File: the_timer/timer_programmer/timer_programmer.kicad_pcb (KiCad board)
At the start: 2 copper layers, 18 x 23.5 mm, 6 parts, among them J1 AVR-ISP-6, J3 R41-B583A, U1 MCP2210x-SS

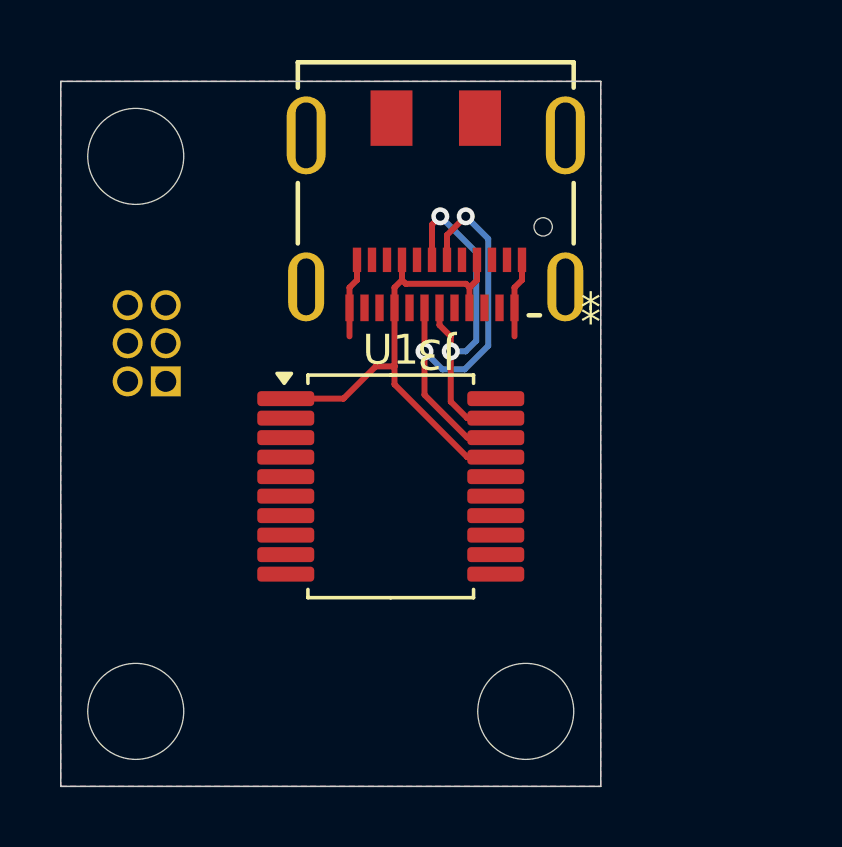
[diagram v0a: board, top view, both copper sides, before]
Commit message: Finished routing Timer Programmer
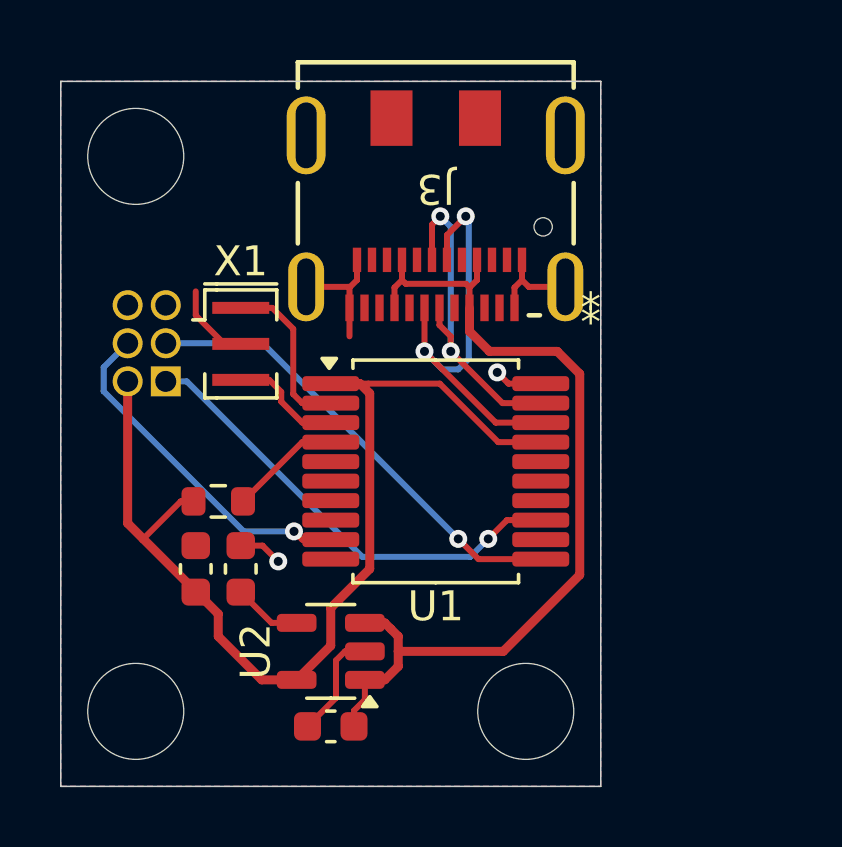
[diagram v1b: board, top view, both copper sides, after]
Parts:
- added C2: 1u, Capacitor_SMD:C_0603_1608Metric, F.Cu at (209.0, 98.0)
- added C3: 0.01u, Capacitor_SMD:C_0603_1608Metric, F.Cu at (206.0, 92.8)
- added C4: 1u, Capacitor_SMD:C_0603_1608Metric, F.Cu at (204.5, 92.8)
- added R1: 10k, Resistor_SMD:R_0603_1608Metric, F.Cu at (205.2, 90.5)
- added U2: TC2185-3.3VxCTTR, Package_TO_SOT_SMD:SOT-23-5, F.Cu at (209.0, 95.5)
- added X1: CSTNE12M0GH5L000R0, Crystal:Resonator_SMD_Murata_CSTxExxV-3Pin_3.0x1.1mm, F.Cu at (206.0, 85.2)
- moved U1 1.58 mm to (212.5, 89.5)
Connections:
- J3 pad A4: VCC -> VBUS
- J3 pad A9: VCC -> VBUS
- J3 pad B4: VCC -> VBUS
- J3 pad B9: VCC -> VBUS
- U1 pad 2: unconnected-(U1-OSC1-Pad2) -> Net-(U1-OSC1)
- U1 pad 3: unconnected-(U1-OSC2-Pad3) -> Net-(U1-OSC2)
- U1 pad 4: ~{RESET} -> Net-(U1-~{RST})
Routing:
- net VBUS: track 0.00 -> 29.9 mm
- net VCC: track 16.8 -> 35.0 mm
- net MISO: track 0.00 -> 16.4 mm, vias 0 -> 1
- net SCLK: track 0.00 -> 15.5 mm, vias 0 -> 1
- net MOSI: track 0.00 -> 12.1 mm, vias 0 -> 1
- net GND: track 5.30 -> 16.8 mm, vias 0 -> 2
- net Net-(U1-OSC1): track 0.00 -> 5.59 mm
- net Net-(U1-OSC2): track 0.00 -> 3.78 mm
- net Net-(U1-~{RST}): track 0.00 -> 3.74 mm
- net Net-(U2-BP): track 0.00 -> 2.29 mm
- net USB_D+: track 12.2 -> 11.5 mm
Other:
- board text added: "${REVISION}"

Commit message: Redesigned Timer Programmer
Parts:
- removed C2, C4: 1u, Capacitor_SMD:C_0603_1608Metric
- removed C3: 0.01u, Capacitor_SMD:C_0603_1608Metric
- removed J3: R41-B583A, locals_but_working_PLEASE:CONN_R41-B583A_MIT
- removed R1: 10k, Resistor_SMD:R_0603_1608Metric
- removed U1: MCP2210x-SS, Package_SO:SSOP-20_5.3x7.2mm_P0.65mm
- removed U2: TC2185-3.3VxCTTR, Package_TO_SOT_SMD:SOT-23-5
- removed X1: CSTNE12M0GH5L000R0, Crystal:Resonator_SMD_Murata_CSTxExxV-3Pin_3.0x1.1mm
- added J2: AVR-ISP-6, Connector_PinHeader_2.54mm:PinHeader_2x03_P2.54mm_Horizontal, F.Cu at (211.3, 86.5)
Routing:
- net VBUS: track 29.9 -> 0.00 mm
- net VCC: track 35.0 -> 13.3 mm, vias 0 -> 1
- net GND: track 16.8 -> 0.00 mm, vias 2 -> 0
- net USB_D-: track 14.7 -> 0.00 mm, vias 2 -> 0
- net ~{RESET}: track 0.00 -> 12.2 mm
- net USB_D+: track 11.5 -> 0.00 mm, vias 2 -> 0
- net Net-(U1-OSC1): track 5.59 -> 0.00 mm
- net MOSI: track 12.1 -> 17.4 mm
- net Net-(U1-OSC2): track 3.78 -> 0.00 mm
- net Net-(U1-~{RST}): track 3.74 -> 0.00 mm
- net Net-(U2-BP): track 2.29 -> 0.00 mm
- net SCLK: track 15.5 -> 17.4 mm
- net MISO: track 16.4 -> 17.4 mm
